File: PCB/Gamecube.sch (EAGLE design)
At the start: 13 parts

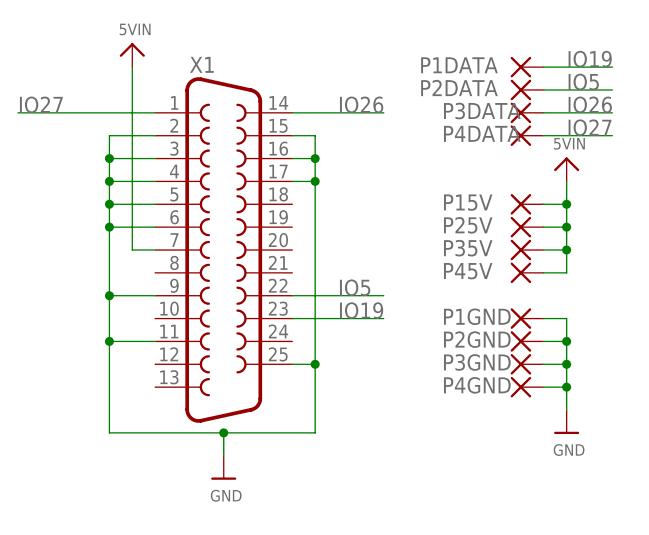
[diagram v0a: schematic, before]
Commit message: Added exposed GND plane at DB25 anchors
All PCBs have been update to have exposed GND plane pads for the DB25 anchor points.

This resolves Issue 54
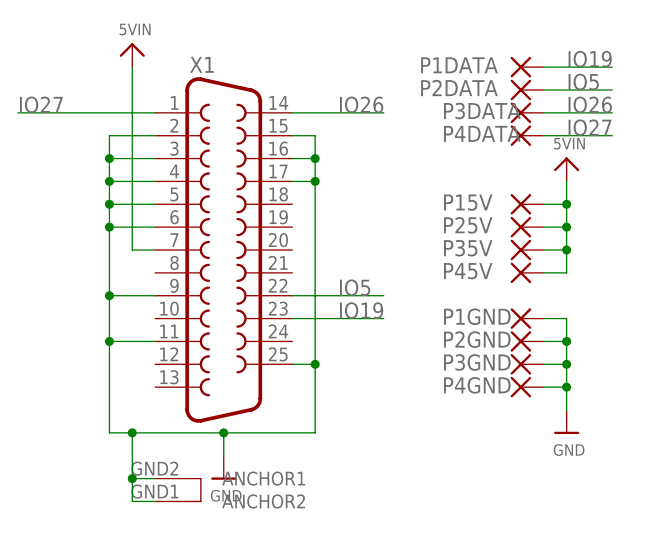
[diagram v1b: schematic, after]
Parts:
- X1: device SparkFun-Retired:DB25_FEMALEH -> SparkFun-Retired:DB25_FEMALEHP
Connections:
- net GND: now also X1.ANCHOR1, X1.ANCHOR2
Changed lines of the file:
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@@
 </classes>
 <parts>
-<part name="X1" library="SparkFun-Retired" deviceset="DB25_FEMALE" device="H"/>
+<part name="X1" library="SparkFun-Retired" deviceset="DB25_FEMALE" device="HP"/>
 <part name="U$53" library="microbuilder" deviceset="VIN" device="" value="5VIN"/>
 <part name="U$54" library="Airquality_Sensor" library_urn="urn:adsk.eagle:library:16015176" deviceset="GND" device=""/>
@@
 <wire x1="414.02" y1="-33.02" x2="414.02" y2="-35.56" width="0.1524" layer="91"/>
 <junction x="414.02" y="-33.02"/>
-<wire x1="414.02" y1="-33.02" x2="401.32" y2="-33.02" width="0.1524" layer="91"/>
+<wire x1="414.02" y1="-33.02" x2="403.86" y2="-33.02" width="0.1524" layer="91"/>
 <pinref part="X1" gate="-1" pin="2"/>
+<wire x1="403.86" y1="-33.02" x2="401.32" y2="-33.02" width="0.1524" layer="91"/>
 <wire x1="406.4" y1="0" x2="401.32" y2="0" width="0.1524" layer="91"/>
 <wire x1="401.32" y1="0" x2="401.32" y2="-2.54" width="0.1524" layer="91"/>
@@
 <wire x1="421.64" y1="-25.4" x2="424.18" y2="-25.4" width="0.1524" layer="91"/>
 <junction x="424.18" y="-25.4"/>
+<wire x1="403.86" y1="-33.02" x2="403.86" y2="-38.1" width="0.1524" layer="91"/>
+<junction x="403.86" y="-33.02"/>
+<pinref part="X1" gate="-1" pin="ANCHOR2"/>
+<wire x1="403.86" y1="-38.1" x2="403.86" y2="-40.64" width="0.1524" layer="91"/>
+<wire x1="403.86" y1="-40.64" x2="406.4" y2="-40.64" width="0.1524" layer="91"/>
+<pinref part="X1" gate="-1" pin="ANCHOR1"/>
+<wire x1="406.4" y1="-38.1" x2="403.86" y2="-38.1" width="0.1524" layer="91"/>
+<junction x="403.86" y="-38.1"/>
 </segment>
 <segment>
